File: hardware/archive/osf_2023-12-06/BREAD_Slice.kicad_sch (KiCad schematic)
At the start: 38 parts, among them J1 Conn_01x10_Female, J2 Term_2, J3 Term_2, J4 Term_2, J6 Term_2, J7 Term_2, J8 Term_2, J9 Term_2, K2 G5Q-1, U1 MCP6001U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

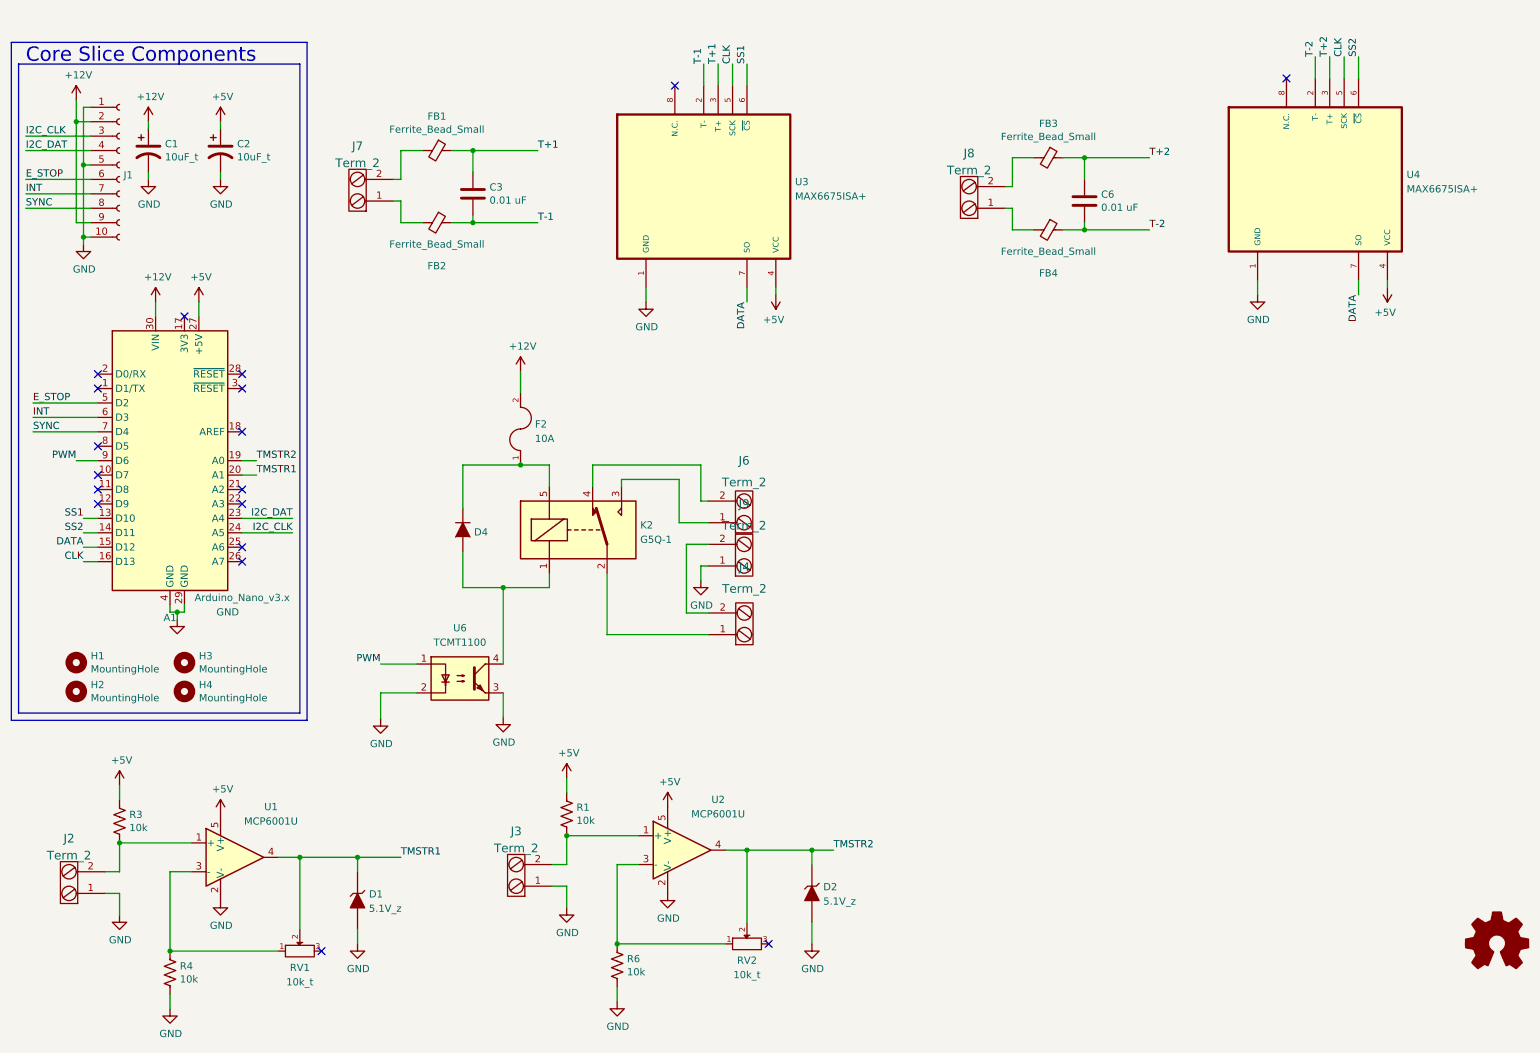
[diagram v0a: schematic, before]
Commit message: added historical scripts and new revisions
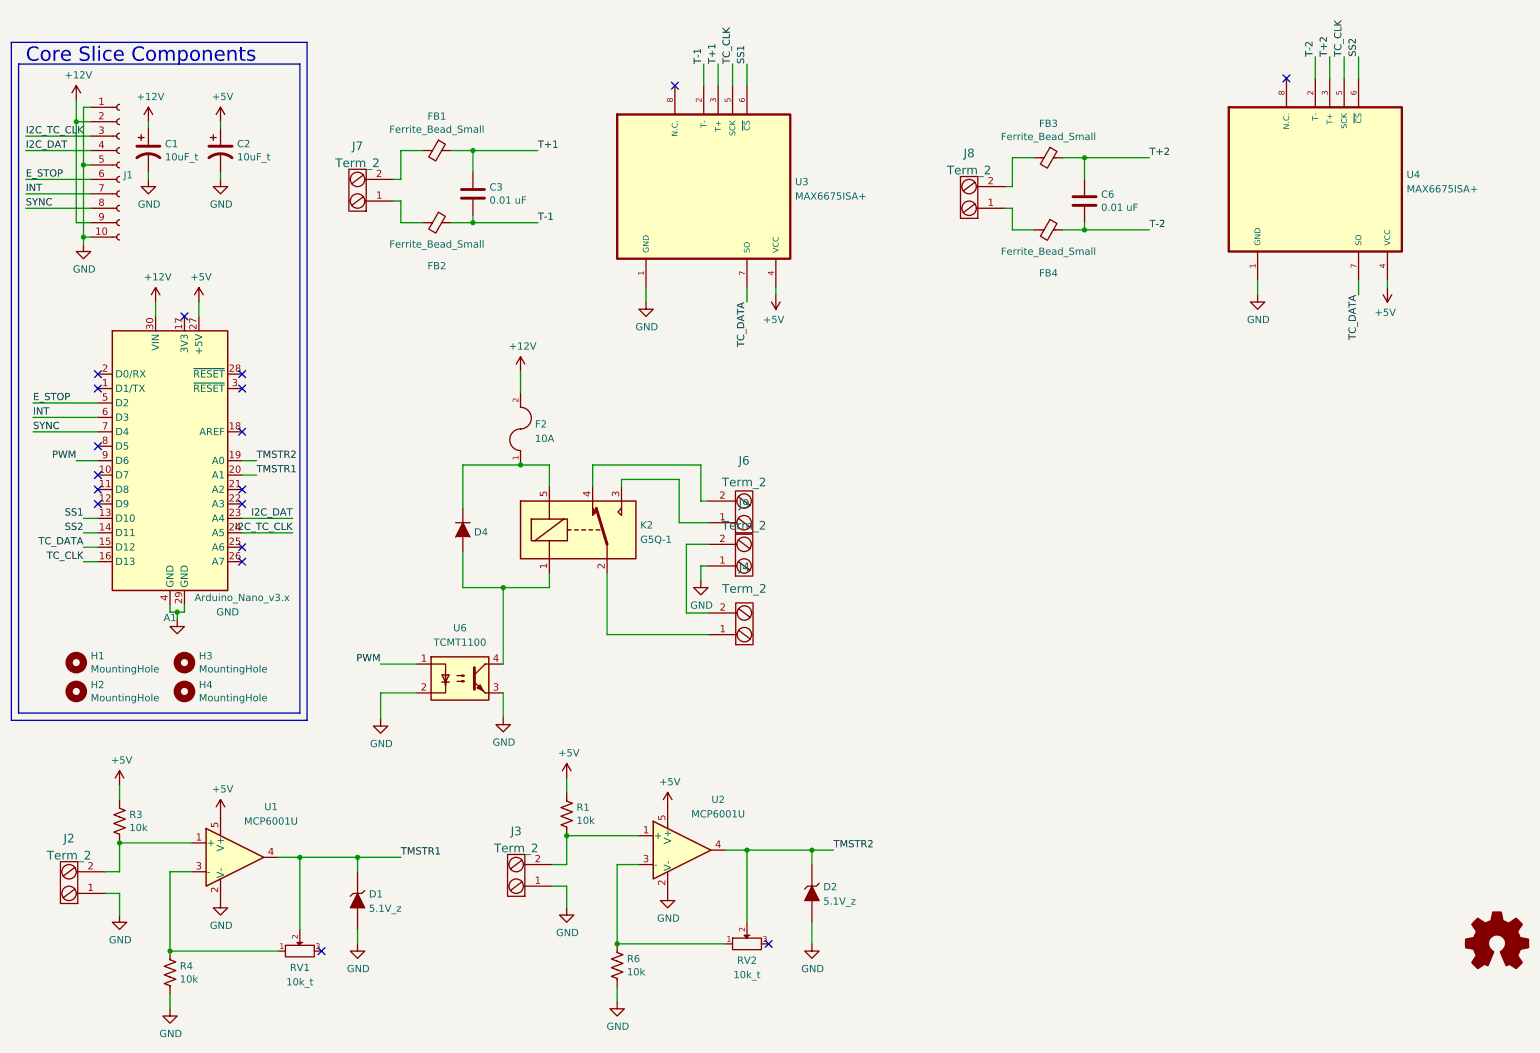
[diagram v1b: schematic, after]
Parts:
- A1: TC_DATAsheet (none) -> http://www.mouser.com/pdfdocs/Gravitech_Arduino_Nano3_0.pdf
- C1, C2: TC_DATAsheet (none) -> https://www.digikey.com/short/qcd8n7
- D1, D2: TC_DATAsheet (none) -> https://www.digikey.com/short/q75wjm
- D4: TC_DATAsheet (none) -> https://www.digikey.com/short/q75wqm
- F2: TC_DATAsheet (none) -> https://www.digikey.com/short/q7wbwz
- J2, J3, J4, J6, J7, J8, J9: TC_DATAsheet (none) -> https://www.digikey.com/short/q7wbhd
- K2: TC_DATAsheet (none) -> https://www.omron.com/ecb/products/pdf/en-g5q.pdf
- RV1, RV2: TC_DATAsheet (none) -> https://www.digikey.com/short/qt5j3q
- U1, U2: TC_DATAsheet (none) -> http://ww1.microchip.com/downloads/en/DeviceDoc/21733j.pdf
- U6: TC_DATAsheet (none) -> http://www.vishay.com/docs/83510/tcmt1100.pdf
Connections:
- net CLK renamed TC_CLK
- net DATA renamed TC_DATA
- net I2C_CLK renamed I2C_TC_CLK
